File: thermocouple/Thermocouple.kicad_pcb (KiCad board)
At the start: 2 copper layers, 50 x 50 mm, 39 parts, among them IC301 nPM1300-QEXX, IC701 MCP9600, M701 BM15C, SW701 Join, X301 Charge, X302 Battery, X701 Debug, X702 Thermocouple

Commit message: Prepare release 1.0.0
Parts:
- moved C301 60.0 mm to (199.2, 160.6)
- moved C303 60.0 mm to (177.8, 153.3)
- moved L301 60.0 mm to (189.4, 160.8)
- moved NT301 60.0 mm to (186.7, 160.0)
- moved R706 60.0 mm to (208.4, 146.2)
- moved C302 60.0 mm to (193.7, 167.3)
- moved C305 60.0 mm to (187.4, 160.9)
- moved C701 60.0 mm to (207.4, 132.0)
- moved C703 60.0 mm to (202.9, 143.9)
- moved C704 60.0 mm to (214.0, 148.0)
- moved D401 60.0 mm to (188.1, 142.9)
- moved FB701 60.0 mm to (211.2, 148.9)
- moved FB702 60.0 mm to (211.2, 147.1)
- moved IC301 60.0 mm to (193.9, 162.1)
- moved IC701 60.0 mm to (202.0, 148.0)
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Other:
- board text removed: "Impedance Table"

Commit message: Update outputs (release)
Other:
- board text added: "1.492mm"
- board text removed: "0.196mm"
- board text removed: "1.03mm"
- board text removed: "Inner1 (GND)"
- board text removed: "Inner2"
- board text removed: "Plane"
- board text removed: "Prepreg"

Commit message: CI/CD improvements, fixing broken PMIC-INT
- Update CI/CD to the latest version
- Move PMIC-INT to port 0 to make it usable

Signed-off-by: Daniel Kampert <DanielKampert@kampis-elektroecke.de>
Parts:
- C301, C302, C303, C304, C305, C306, C307, C701, C703, C704: footprint Resistor_SMD:R_0805_2012Metric -> Capacitor_SMD:C_0805_2012Metric
- L301: footprint Resistor_SMD:R_0805_2012Metric -> Inductor_SMD_Kampi:L_0806_2016
- moved C302 0.10 mm to (193.7, 167.4)
- moved R301 0.10 mm to (195.7, 167.4)
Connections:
- IC701 pad 10: (no net) -> unconnected-(IC701-NC-Pad10)
- IC701 pad 13: (no net) -> unconnected-(IC701-NC-Pad13)
- IC701 pad 17: (no net) -> unconnected-(IC701-NC-Pad17)
- IC701 pad 18: (no net) -> unconnected-(IC701-NC-Pad18)
- IC701 pad 3: (no net) -> unconnected-(IC701-NC-Pad3)
- IC701 pad 5: (no net) -> unconnected-(IC701-NC-Pad5)
- IC701 pad 6: (no net) -> unconnected-(IC701-NC-Pad6)
- IC701 pad 7: (no net) -> unconnected-(IC701-NC-Pad7)
- IC701 pad 9: (no net) -> unconnected-(IC701-NC-Pad9)
- M701 pad H9: /Project Architecture/Main/PMIC-INT -> unconnected-(M701-P2.00-PadH9)_1
- M701 pad J4: unconnected-(M701-P0.00-PadJ4) -> /Project Architecture/Main/PMIC-INT
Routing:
- net /Project Architecture/Main/PMIC-INT: track 37.4 -> 42.3 mm
- net /Project Architecture/Main/SCL: track 79.0 -> 78.3 mm
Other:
- board text added: "0.196mm"
- board text added: "1.03mm"
- board text added: "Inner1 (GND)"
- board text added: "Inner2"
- board text added: "Plane"
- board text added: "Prepreg"
- board text removed: "1.492mm"

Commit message: Reduce the brightnes of the status LED, use VSys for the LEDs
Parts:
- R401: value 590R -> 4k7
- R402: value 430R -> 10k
- R403: value 430R -> 3k3
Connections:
- C301 pad 1: Net-(D401-A) -> Net-(IC301-V_{BUS})
- D401 pad 1: Net-(D401-A) -> /Project Architecture/Power/VSYS
- IC301 pad 21: Net-(D401-A) -> Net-(IC301-V_{BUS})
- X301 pad A4: Net-(D401-A) -> Net-(IC301-V_{BUS})
- X301 pad A9: Net-(D401-A) -> Net-(IC301-V_{BUS})
- X301 pad B4: Net-(D401-A) -> Net-(IC301-V_{BUS})
- X301 pad B9: Net-(D401-A) -> Net-(IC301-V_{BUS})
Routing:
- net Net-(D401-A): track 58.6 -> 0.00 mm, vias 5 -> 0
- net Net-(IC301-V_{BUS}): track 0.00 -> 29.0 mm, vias 0 -> 3
- net /Project Architecture/Power/VSYS: track 21.1 -> 46.1 mm, vias 2 -> 5
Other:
- board text added: "+"
- board text added: "-"

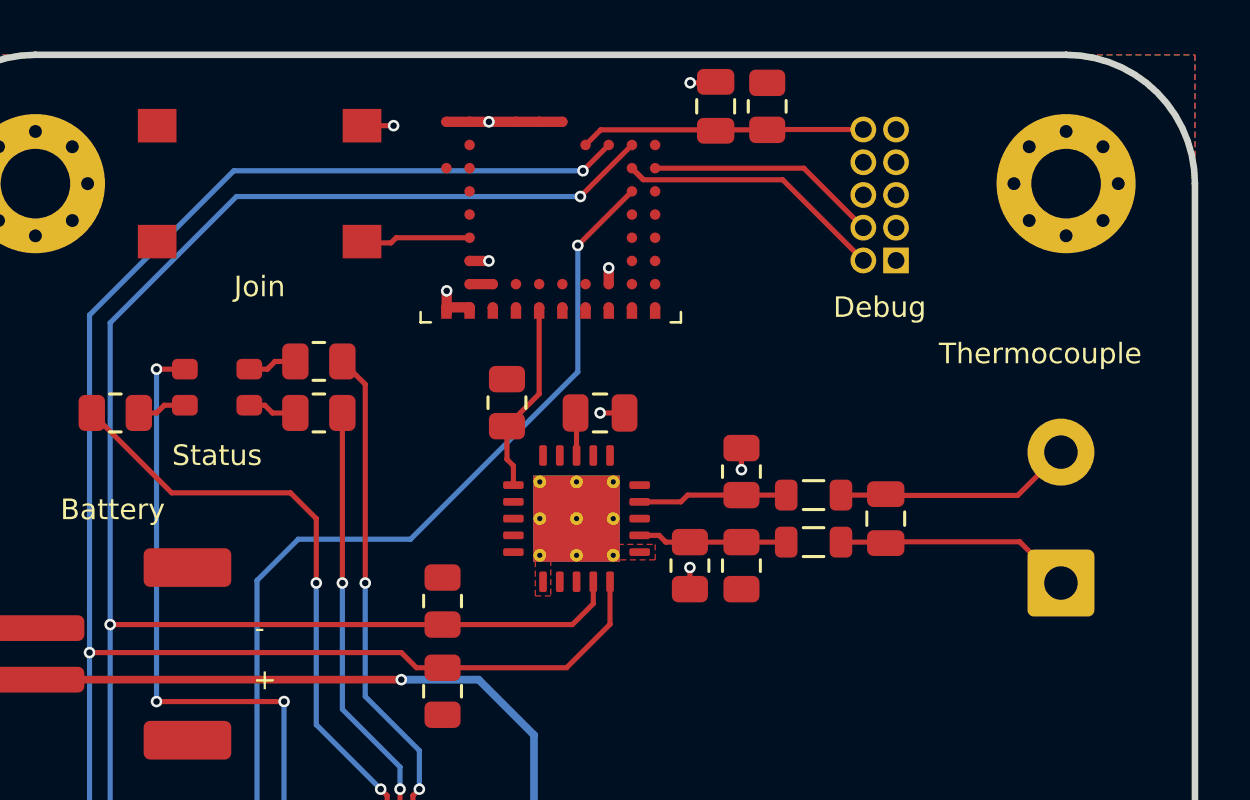
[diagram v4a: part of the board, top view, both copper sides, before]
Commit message: Change thermocouple connector to a different type
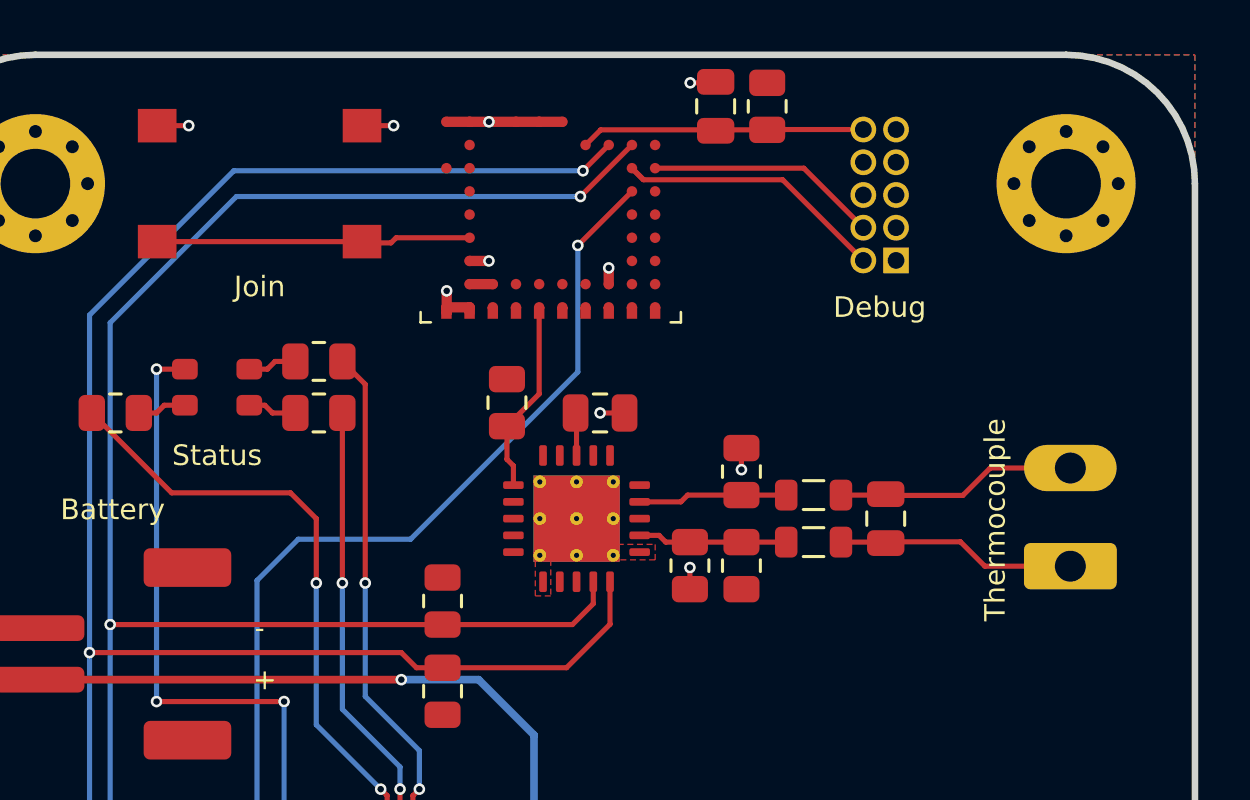
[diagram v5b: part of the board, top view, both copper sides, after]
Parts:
- X702: footprint TerminalBlock_Phoenix:TerminalBlock_Phoenix_MKDS-1,5-2-5.08_1x02_P5.08mm_Horizontal -> Connector_Phoenix_MC:PhoenixContact_MC_1,5_2-G-3.81_1x02_P3.81mm_Horizontal
- moved X702 0.75 mm to (221.2, 149.8)
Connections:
- SW701 pad 3: (no net) -> Net-(M701-P1.14/AIN7)
- SW701 pad 4: (no net) -> GND
- X301 pad A8: (no net) -> unconnected-(X301-SBU1-PadA8)
- X301 pad B8: (no net) -> unconnected-(X301-SBU2-PadB8)
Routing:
- net Net-(M701-P1.14/AIN7): track 4.21 -> 12.2 mm
- net GND: track 35.3 -> 36.5 mm, vias 21 -> 22
